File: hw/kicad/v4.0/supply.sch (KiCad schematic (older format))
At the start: 65 parts, among them P3 CONN_01X02, U13 ACT4088, U2 zldo1117, U27 ACT4088, U28 ACT4088

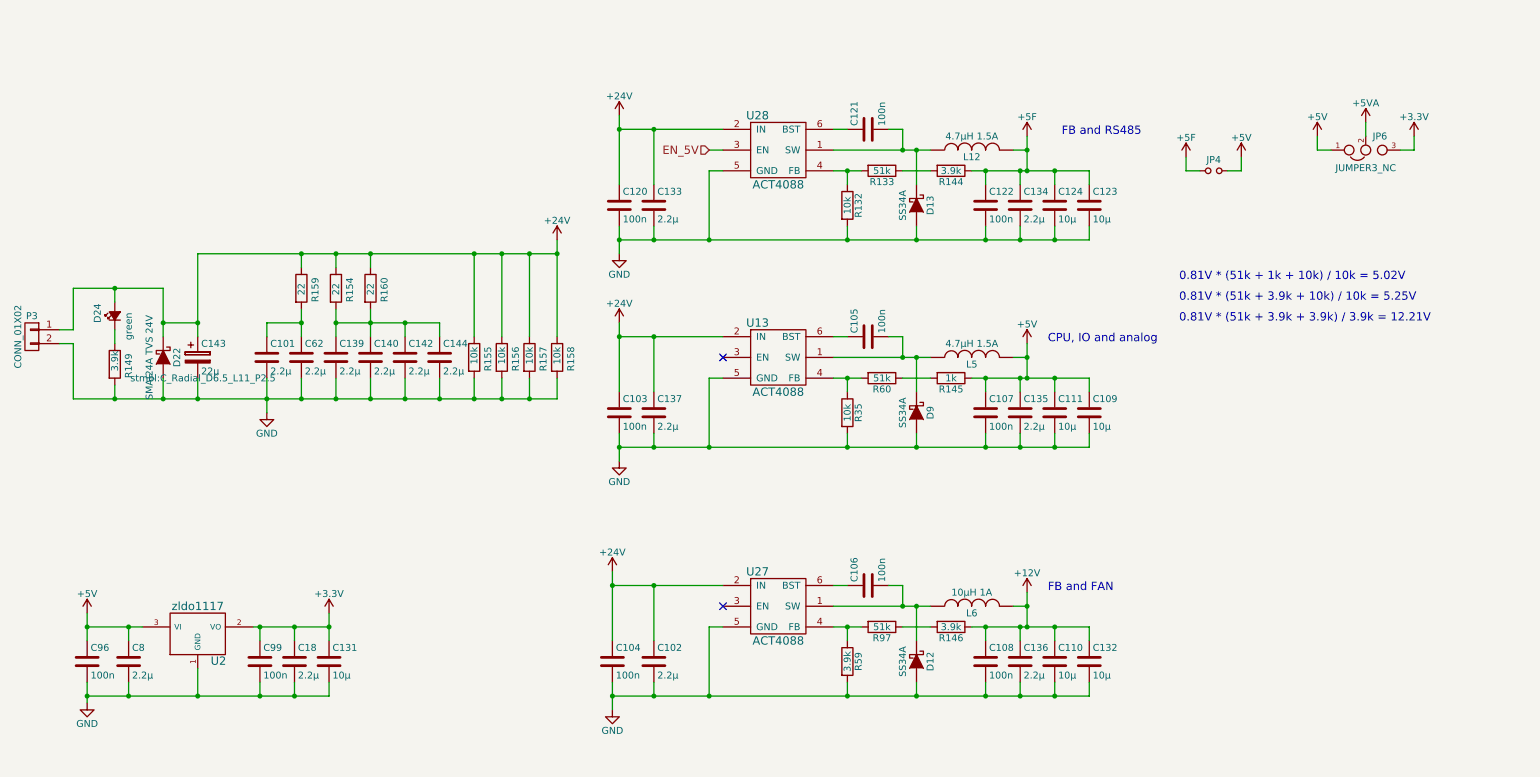
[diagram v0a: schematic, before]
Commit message: changes for IKCM30F60GD
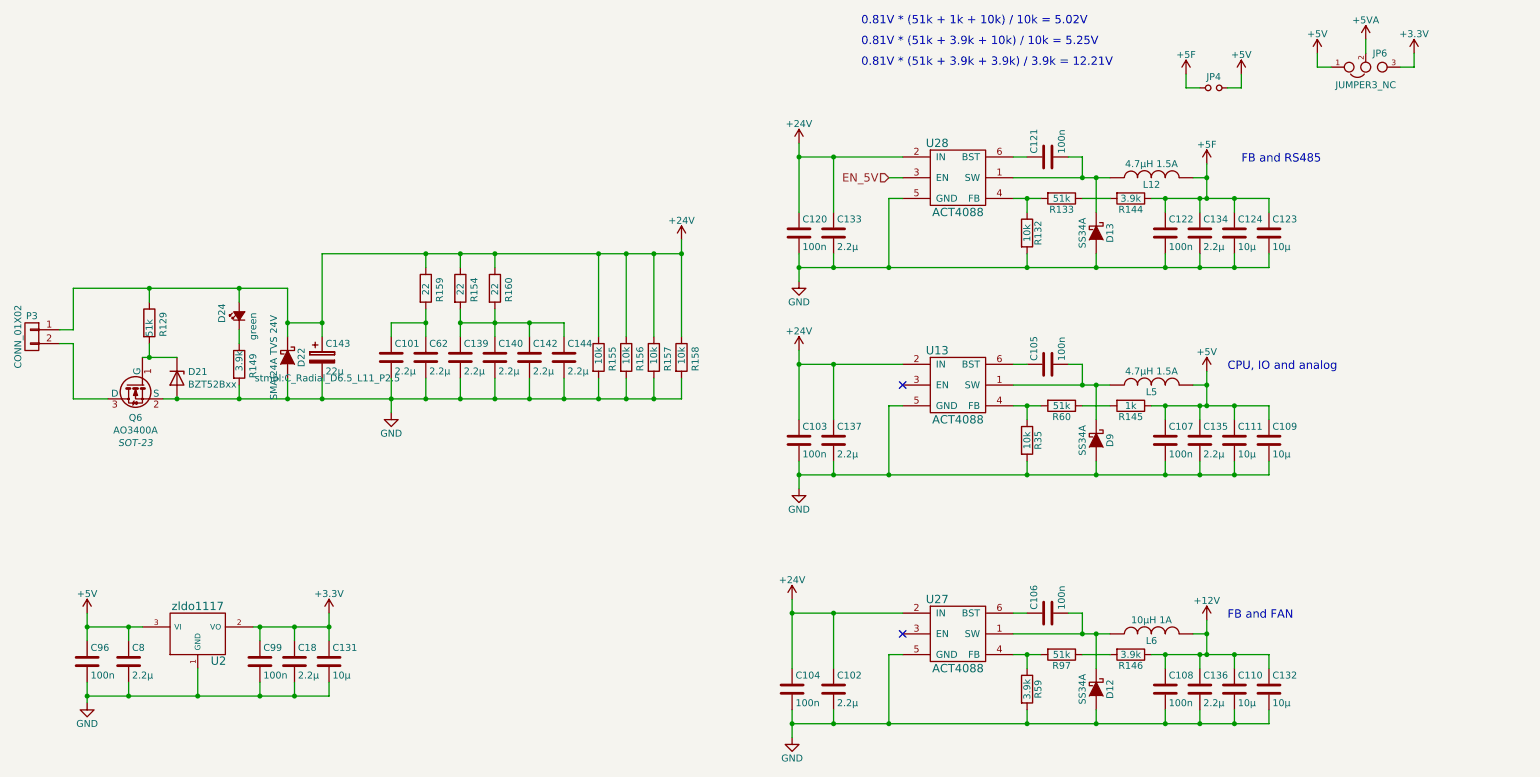
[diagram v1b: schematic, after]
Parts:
- added D21: BZT52Bxx, Diode_SMD:D_SOD-123, symbol Diode:BZT52Bxx
- added Q6: AO3400A, SOT-23, symbol stmbl:MMBF170
- added R129: 51k, stmbl:R_0603, symbol stmbl:R
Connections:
- net +24V: now also R129.1
- net GND: now also D21.2 (A), Q6.2 (S); no longer P3.2 (P2)
- new net: P3.2 (P2), Q6.3 (D)
- new net: D21.1 (K), Q6.1 (G), R129.2
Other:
- moved on the sheet: C101, C102, C103, C104, C105, C106, C107, C108, C109, C110, C111, C120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
